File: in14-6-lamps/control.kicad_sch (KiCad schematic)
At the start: 22 parts, among them J2 Conn_01x02_Pin, J3 Conn_01x06_Pin, Q10 2N7002, SW1 SW_Push, U3 ESP32-WROOM-32D, U4 DS3231M, U5 74141

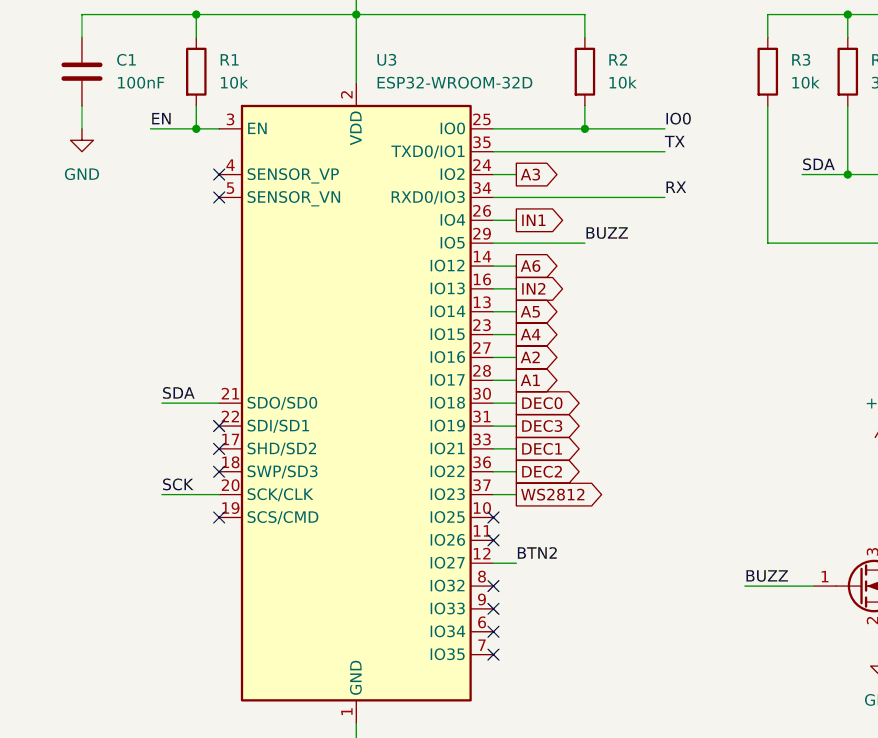
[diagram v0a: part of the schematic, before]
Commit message: fix i2c connection
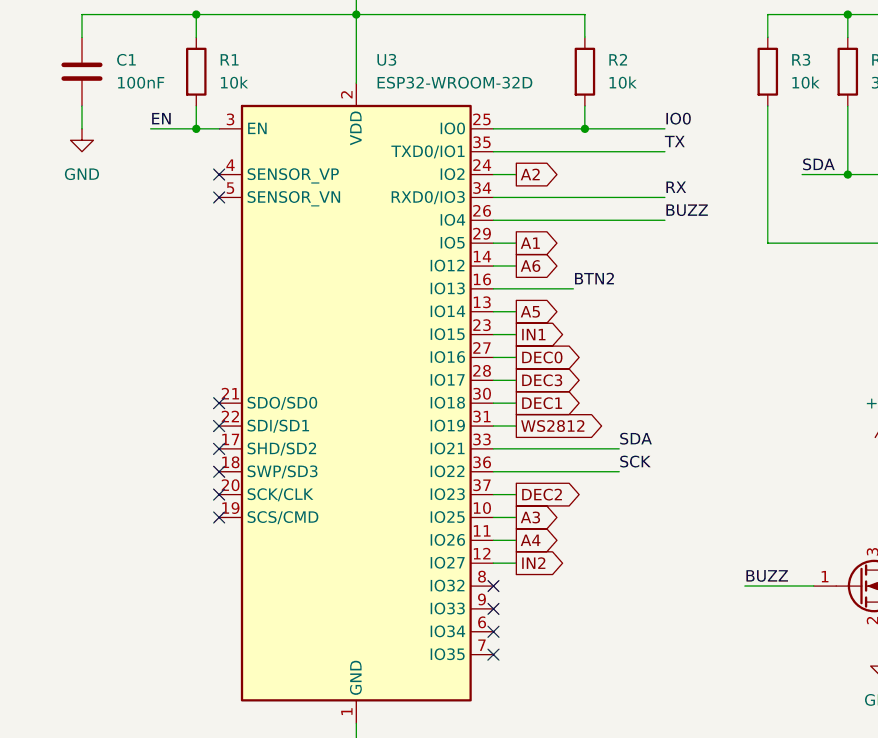
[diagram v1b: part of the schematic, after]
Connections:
- net A1: now also U3.29 (IO5); no longer U3.28 (IO17)
- net A2: now also U3.24 (IO2); no longer U3.27 (IO16)
- net A3: now also U3.10 (IO25); no longer U3.24 (IO2)
- net A4: now also U3.11 (IO26); no longer U3.23 (IO15)
- net BTN2: now also U3.16 (IO13); no longer U3.12 (IO27)
- net BUZZ: now also U3.26 (IO4); no longer U3.29 (IO5)
- net DEC0: now also U3.27 (IO16); no longer U3.30 (IO18)
- net DEC1: now also U3.30 (IO18); no longer U3.33 (IO21)
- net DEC2: now also U3.37 (IO23); no longer U3.36 (IO22)
- net DEC3: now also U3.28 (IO17); no longer U3.31 (IO19)
- net IN1: now also U3.23 (IO15); no longer U3.26 (IO4)
- net IN2: now also U3.12 (IO27); no longer U3.16 (IO13)
- net SCK: now also U3.36 (IO22); no longer U3.20 (SCK/CLK)
- net SDA: now also U3.33 (IO21); no longer U3.21 (SDO/SD0)
- net WS2812: now also U3.31 (IO19); no longer U3.37 (IO23)

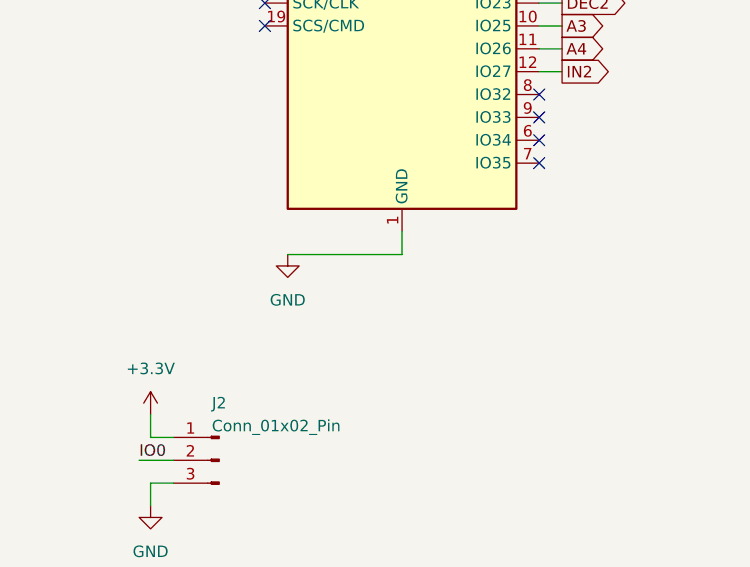
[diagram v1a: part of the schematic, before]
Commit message: fix i2c connection
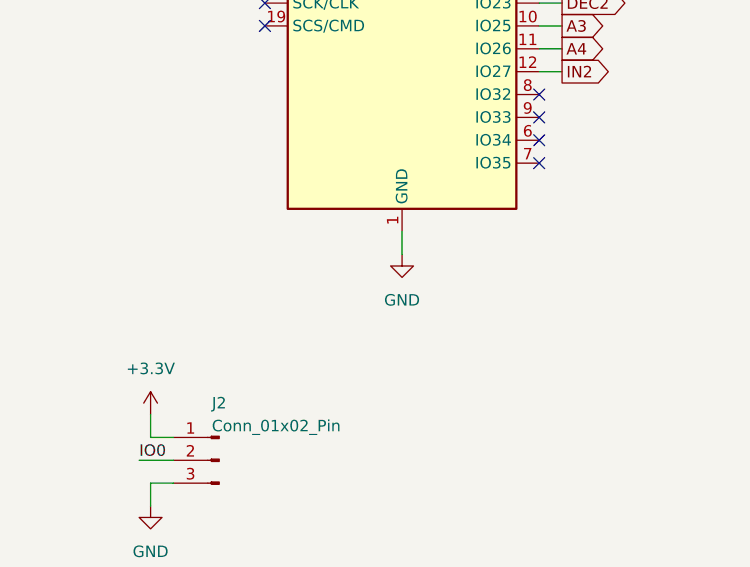
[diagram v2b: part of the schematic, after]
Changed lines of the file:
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@@
 	(wire
 		(pts
-			(xy 63.5 111.76) (xy 50.8 111.76)
-		)
-		(stroke
-			(width 0)
-			(type default)
-		)
-	)
-	(wire
-		(pts
 			(xy 251.46 76.2) (xy 254 76.2)
 		)
@@
 	(symbol
 		(lib_id "power:GND")
-		(at 50.8 111.76 0)
+		(at 63.5 111.76 0)
 		(unit 1)
 		(exclude_from_sim no)
@@
 		(fields_autoplaced yes)
 		(property "Reference" "#PWR09"
-			(at 50.8 118.11 0)
+			(at 63.5 118.11 0)
 			(effects
 				(font
@@
 		)
 		(property "Value" "GND"
-			(at 50.8 116.84 0)
+			(at 63.5 116.84 0)
 			(effects
 				(font
@@
 		)
 		(property "Footprint" ""
-			(at 50.8 111.76 0)
+			(at 63.5 111.76 0)
 			(effects
 				(font
@@
 		)
 		(property "Datasheet" ""
-			(at 50.8 111.76 0)
+			(at 63.5 111.76 0)
 			(effects
 				(font
@@
 		)
 		(property "Description" "Power symbol creates a global label with name \"GND\" , ground"
-			(at 50.8 111.76 0)
+			(at 63.5 111.76 0)
 			(effects
 				(font
